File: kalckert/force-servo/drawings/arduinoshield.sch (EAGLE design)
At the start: 20 parts, among them IC1 MCP604P, IC2 7806L

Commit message: Finnished PC board
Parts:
- added X3, X4: (no value), con-phoenix-254:MPT2
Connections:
- net GND: now also X3-1.1, X4-1.1
- net LED_GREEN: now also X3-2.1
- net LED_RED: now also X4-2.1
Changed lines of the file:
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@@
 <part name="R3" library="resistor" deviceset="R-EU_" device="0207/7" value="10k"/>
 <part name="R4" library="resistor" deviceset="R-EU_" device="0207/7" value="10k"/>
+<part name="X3" library="con-phoenix-254" deviceset="MPT2" device="">
+<attribute name="MF" value=""/>
+<attribute name="MPN" value=""/>
+<attribute name="OC_FARNELL" value="unknown"/>
+<attribute name="OC_NEWARK" value="unknown"/>
+</part>
+<part name="X4" library="con-phoenix-254" deviceset="MPT2" device="">
+<attribute name="MF" value=""/>
+<attribute name="MPN" value=""/>
+<attribute name="OC_FARNELL" value="unknown"/>
+<attribute name="OC_NEWARK" value="unknown"/>
+</part>
+<part name="GND5" library="supply1" deviceset="GND" device=""/>
+<part name="GND7" library="supply1" deviceset="GND" device=""/>
 </parts>
 <sheets>
 <sheet>
 <plain>
-<text x="86.36" y="15.24" size="1.778" layer="91">Shield for the Arduino Board</text>
+<text x="205.74" y="20.32" size="1.778" layer="94" font="vector" rot="MR0">Shield for the Arduino Board</text>
 </plain>
 <instances>
@@
 <instance part="R3" gate="G$1" x="195.58" y="114.3"/>
 <instance part="R4" gate="G$1" x="195.58" y="111.76"/>
+<instance part="X3" gate="-1" x="243.84" y="114.3" rot="MR180"/>
+<instance part="X3" gate="-2" x="243.84" y="119.38" smashed="yes" rot="MR180">
+<attribute name="NAME" x="247.396" y="120.015" size="1.778" layer="95" rot="MR180"/>
+<attribute name="VALUE" x="242.824" y="122.682" size="1.778" layer="96" rot="MR180"/>
+</instance>
+<instance part="X4" gate="-1" x="243.84" y="96.52" rot="MR180"/>
+<instance part="X4" gate="-2" x="243.84" y="101.6" smashed="yes" rot="MR180">
+<attribute name="NAME" x="247.396" y="102.235" size="1.778" layer="95" rot="MR180"/>
+<attribute name="VALUE" x="242.824" y="104.902" size="1.778" layer="96" rot="MR180"/>
+</instance>
+<instance part="GND5" gate="1" x="238.76" y="91.44"/>
+<instance part="GND7" gate="1" x="238.76" y="109.22"/>
 </instances>
 <busses>
@@
 <wire x1="73.66" y1="101.6" x2="73.66" y2="99.06" width="0.1524" layer="91"/>
 </segment>
+<segment>
+<pinref part="X4" gate="-1" pin="1"/>
+<wire x1="241.3" y1="96.52" x2="238.76" y2="96.52" width="0.1524" layer="91"/>
+<wire x1="238.76" y1="96.52" x2="238.76" y2="93.98" width="0.1524" layer="91"/>
+<pinref part="GND5" gate="1" pin="GND"/>
+</segment>
+<segment>
+<pinref part="X3" gate="-1" pin="1"/>
+<wire x1="241.3" y1="114.3" x2="238.76" y2="114.3" width="0.1524" layer="91"/>
+<wire x1="238.76" y1="114.3" x2="238.76" y2="111.76" width="0.1524" layer="91"/>
+<pinref part="GND7" gate="1" pin="GND"/>
+</segment>
 </net>
 <net name="VCCSERVO" class="0">
@@
 <label x="203.2" y="114.3" size="1.778" layer="95"/>
 </segment>
+<segment>
+<pinref part="X3" gate="-2" pin="1"/>
+<wire x1="241.3" y1="119.38" x2="238.76" y2="119.38" width="0.1524" layer="91"/>
+<label x="223.52" y="119.38" size="1.778" layer="95"/>
+</segment>
 </net>
 <net name="LED_RED" class="0">
@@
 <label x="203.2" y="111.76" size="1.778" layer="95"/>
 </segment>
-</net>
+<segment>
+<pinref part="X4" gate="-2" pin="1"/>
+<wire x1="241.3" y1="101.6" x2="238.76" y2="101.6" width="0.1524" layer="91"/>
+<label x="223.52" y="101.6" size="1.778" layer="95"/>
+</segment>
+</net>

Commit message: First version of the PCB is ready.
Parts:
- removed 7905: 7905, linear:7905L
- removed IC2: 7806L, linear:7806L
- added IC3: 7806T, linear:7806T
- added IC4: (no value), linear:7905T
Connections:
- net -9V: now also IC4.GND; no longer 7905.GND
- net BUZZER: now also DIGITALPIN0-7.4; no longer DIGITALPIN0-7.1
- net GND: now also IC4.VO; no longer 7905.VO
- net N$1: now also DIGITALPIN0-7.1; no longer DIGITALPIN0-7.3
- net N$2: now also IC4.VI; no longer 7905.VI
- net N$3: now also IC3.GND; no longer IC2.GND
- net N$4: now also DIGITALPIN0-7.2; no longer DIGITALPIN0-7.4
- net VCCSERVO: now also IC3.VO; no longer IC2.VO
- net VIN: now also IC3.VI; no longer IC2.VI
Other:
- moved on the sheet: R3, R4
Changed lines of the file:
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@@
 <setting verticaltext="up"/>
 </settings>
-<grid distance="0.1" unitdist="inch" unit="inch" style="lines" multiple="1" display="yes" altdistance="0.01" altunitdist="inch" altunit="inch"/>
+<grid distance="0.1" unitdist="inch" unit="inch" style="lines" multiple="1" display="no" altdistance="0.01" altunitdist="inch" altunit="inch"/>
 <layers>
 <layer number="1" name="Top" color="4" fill="1" visible="no" active="no"/>
@@
 <part name="SG1" library="buzzer" deviceset="F/HMB" device=""/>
 <part name="IC1" library="linear" deviceset="MCP604" device="P"/>
-<part name="7905" library="linear" deviceset="79*" device="L" technology="05" value="7905"/>
 <part name="R1" library="pot" deviceset="TRIM_EU-" device="S64W"/>
 <part name="C1" library="rcl" deviceset="C-EU" device="025-025X050" value="330nF"/>
@@
 <part name="GND2" library="supply1" deviceset="GND" device=""/>
 <part name="GND4" library="supply1" deviceset="GND" device=""/>
-<part name="IC2" library="linear" deviceset="78*" device="L" technology="06"/>
 <part name="C3" library="rcl" deviceset="C-EU" device="025-025X050" value="330nF"/>
 <part name="C4" library="rcl" deviceset="C-EU" device="025-025X050" value="100nF"/>
@@
 <part name="GND5" library="supply1" deviceset="GND" device=""/>
 <part name="GND7" library="supply1" deviceset="GND" device=""/>
+<part name="IC3" library="linear" deviceset="78*" device="T" technology="06"/>
+<part name="IC4" library="linear" deviceset="79*" device="T" technology="05"/>
 </parts>
 <sheets>
@@
 <instance part="IC1" gate="C" x="170.18" y="35.56"/>
 <instance part="IC1" gate="D" x="198.12" y="35.56"/>
-<instance part="7905" gate="A1" x="53.34" y="33.02"/>
 <instance part="R1" gate="1" x="99.06" y="152.4" rot="R270"/>
 <instance part="C1" gate="G$1" x="33.02" y="35.56"/>
@@
 <instance part="GND2" gate="1" x="73.66" y="96.52"/>
 <instance part="GND4" gate="1" x="142.24" y="66.04"/>
-<instance part="IC2" gate="A1" x="53.34" y="63.5"/>
 <instance part="C3" gate="G$1" x="33.02" y="60.96"/>
 <instance part="C4" gate="G$1" x="68.58" y="60.96"/>
-<instance part="GND3" gate="1" x="53.34" y="53.34"/>
+<instance part="GND3" gate="1" x="53.34" y="48.26"/>
 <instance part="GND6" gate="1" x="68.58" y="27.94"/>
-<instance part="R3" gate="G$1" x="195.58" y="114.3"/>
-<instance part="R4" gate="G$1" x="195.58" y="111.76"/>
+<instance part="R3" gate="G$1" x="195.58" y="119.38"/>
+<instance part="R4" gate="G$1" x="195.58" y="116.84"/>
 <instance part="X3" gate="-1" x="243.84" y="114.3" rot="MR180"/>
 <instance part="X3" gate="-2" x="243.84" y="119.38" smashed="yes" rot="MR180">
@@
 <instance part="GND5" gate="1" x="238.76" y="91.44"/>
 <instance part="GND7" gate="1" x="238.76" y="109.22"/>
+<instance part="IC3" gate="A1" x="53.34" y="63.5"/>
+<instance part="IC4" gate="A1" x="53.34" y="33.02"/>
 </instances>
 <busses>
@@
 <wire x1="33.02" y1="38.1" x2="53.34" y2="38.1" width="0.1524" layer="91"/>
 <junction x="33.02" y="38.1"/>
-<pinref part="7905" gate="A1" pin="GND"/>
-<junction x="53.34" y="38.1"/>
+<junction x="68.58" y="38.1"/>
 <wire x1="53.34" y1="38.1" x2="68.58" y2="38.1" width="0.1524" layer="91"/>
-<junction x="68.58" y="38.1"/>
 <wire x1="68.58" y1="38.1" x2="76.2" y2="38.1" width="0.1524" layer="91"/>
 <label x="76.2" y="38.1" size="1.778" layer="95"/>
 <wire x1="33.02" y1="38.1" x2="27.94" y2="38.1" width="0.1524" layer="91"/>
+<pinref part="IC4" gate="A1" pin="GND"/>
+<junction x="53.34" y="38.1"/>
 </segment>
 <segment>
@@
 <pinref part="C1" gate="G$1" pin="2"/>
 <pinref part="BATTERY" gate="-2" pin="1"/>
-<pinref part="7905" gate="A1" pin="VI"/>
 <wire x1="33.02" y1="30.48" x2="43.18" y2="30.48" width="0.1524" layer="91"/>
 <junction x="33.02" y="30.48"/>
 <wire x1="33.02" y1="30.48" x2="27.94" y2="30.48" width="0.1524" layer="91"/>
+<pinref part="IC4" gate="A1" pin="VI"/>
 </segment>
 </net>
@@
 <segment>
 <pinref part="C2" gate="G$1" pin="2"/>
-<pinref part="7905" gate="A1" pin="VO"/>
 <wire x1="68.58" y1="30.48" x2="63.5" y2="30.48" width="0.1524" layer="91"/>
 <junction x="68.58" y="30.48"/>
 <pinref part="GND6" gate="1" pin="GND"/>
+<pinref part="IC4" gate="A1" pin="VO"/>
 </segment>
 <segment>
@@
 </segment>
 <segment>
-<pinref part="IC2" gate="A1" pin="VO"/>
 <wire x1="63.5" y1="63.5" x2="68.58" y2="63.5" width="0.1524" layer="91"/>
 <pinref part="C4" gate="G$1" pin="1"/>
@@
 <junction x="68.58" y="63.5"/>
 <label x="73.66" y="63.5" size="1.778" layer="95"/>
+<pinref part="IC3" gate="A1" pin="VO"/>
 </segment>
 </net>
@@
 </segment>
 <segment>
-<pinref part="DIGITALPIN0-7" gate="A" pin="1"/>
-<wire x1="185.42" y1="119.38" x2="195.58" y2="119.38" width="0.1524" layer="91"/>
-<label x="195.58" y="119.38" size="1.778" layer="95"/>
+<pinref part="DIGITALPIN0-7" gate="A" pin="4"/>
+<wire x1="185.42" y1="111.76" x2="203.2" y2="111.76" width="0.1524" layer="91"/>
+<label x="203.2" y="111.76" size="1.778" layer="95"/>
 </segment>
 </net>
@@
 </segment>
 <segment>
-<pinref part="IC2" gate="A1" pin="VI"/>
 <wire x1="43.18" y1="63.5" x2="33.02" y2="63.5" width="0.1524" layer="91"/>
 <pinref part="C3" gate="G$1" pin="1"/>
@@
 <junction x="33.02" y="63.5"/>
 <label x="25.4" y="63.5" size="1.778" layer="95"/>
+<pinref part="IC3" gate="A1" pin="VI"/>
 </segment>
 </net>
 <net name="N$3" class="0">
 <segment>
+<pinref part="GND3" gate="1" pin="GND"/>
+<pinref part="IC3" gate="A1" pin="GND"/>
+<wire x1="53.34" y1="50.8" x2="53.34" y2="53.34" width="0.1524" layer="91"/>
 <pinref part="C3" gate="G$1" pin="2"/>
-<wire x1="33.02" y1="55.88" x2="53.34" y2="55.88" width="0.1524" layer="91"/>
+<wire x1="53.34" y1="53.34" x2="53.34" y2="55.88" width="0.1524" layer="91"/>
+<wire x1="33.02" y1="55.88" x2="33.02" y2="53.34" width="0.1524" layer="91"/>
 <pinref part="C4" gate="G$1" pin="2"/>
-<pinref part="GND3" gate="1" pin="GND"/>
-<wire x1="53.34" y1="55.88" x2="68.58" y2="55.88" width="0.1524" layer="91"/>
-<junction x="53.34" y="55.88"/>
-<pinref part="IC2" gate="A1" pin="GND"/>
-</segment>
-</net>
-<net name="N$4" class="0">
-<segment>
-<pinref part="R4" gate="G$1" pin="1"/>
-<pinref part="DIGITALPIN0-7" gate="A" pin="4"/>
-<wire x1="190.5" y1="111.76" x2="185.42" y2="111.76" width="0.1524" layer="91"/>
+<wire x1="33.02" y1="53.34" x2="53.34" y2="53.34" width="0.1524" layer="91"/>
+<wire x1="53.34" y1="53.34" x2="68.58" y2="53.34" width="0.1524" layer="91"/>
+<wire x1="68.58" y1="53.34" x2="68.58" y2="55.88" width="0.1524" layer="91"/>
+<junction x="53.34" y="53.34"/>
 </segment>
 </net>
@@
 <segment>
 <pinref part="R3" gate="G$1" pin="2"/>
-<wire x1="200.66" y1="114.3" x2="203.2" y2="114.3" width="0.1524" layer="91"/>
-<label x="203.2" y="114.3" size="1.778" layer="95"/>
+<wire x1="200.66" y1="119.38" x2="203.2" y2="119.38" width="0.1524" layer="91"/>
+<label x="203.2" y="119.38" size="1.778" layer="95"/>
 </segment>
 <segment>
@@
 <segment>
 <pinref part="R4" gate="G$1" pin="2"/>
-<wire x1="200.66" y1="111.76" x2="203.2" y2="111.76" width="0.1524" layer="91"/>
-<label x="203.2" y="111.76" size="1.778" layer="95"/>
+<wire x1="200.66" y1="116.84" x2="203.2" y2="116.84" width="0.1524" layer="91"/>
+<label x="203.2" y="116.84" size="1.778" layer="95"/>
 </segment>
 <segment>
@@
 <segment>
 <pinref part="R3" gate="G$1" pin="1"/>
-<pinref part="DIGITALPIN0-7" gate="A" pin="3"/>
-<wire x1="190.5" y1="114.3" x2="185.42" y2="114.3" width="0.1524" layer="91"/>
-</segment>
-</net>
+<pinref part="DIGITALPIN0-7" gate="A" pin="1"/>
+<wire x1="190.5" y1="119.38" x2="185.42" y2="119.38" width="0.1524" layer="91"/>
+</segment>
+</net>
+<net name="N$4" class="0">
+<segment>
+<pinref part="DIGITALPIN0-7" gate="A" pin="2"/>
+<pinref part="R4" gate="G$1" pin="1"/>
+<wire x1="185.42" y1="116.84" x2="190.5" y2="116.84" width="0.1524" layer="91"/>
+</segment>
+</net>

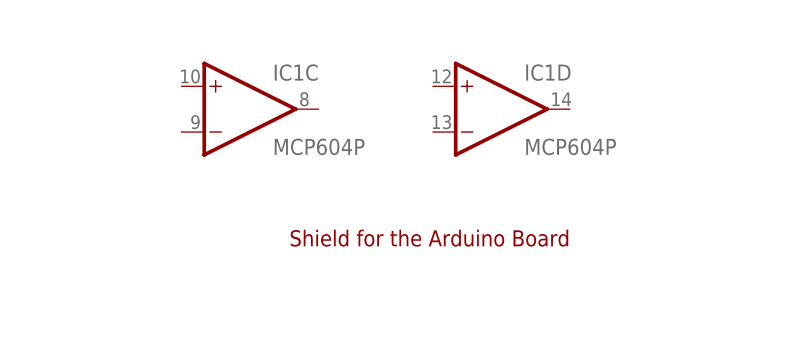
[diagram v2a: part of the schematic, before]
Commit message: Added licensing info to board. Tested python program on mac (tkinter only works in IDLE).
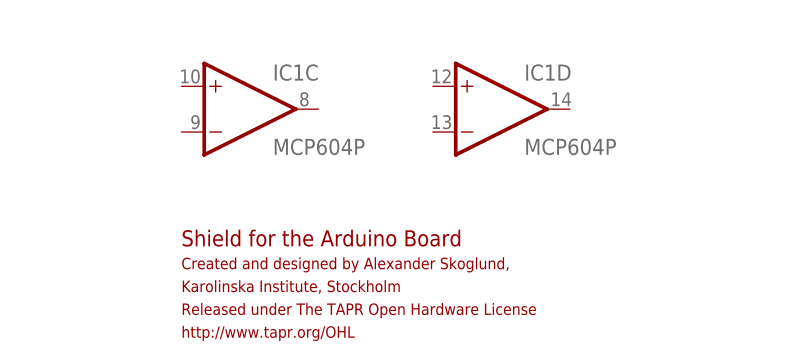
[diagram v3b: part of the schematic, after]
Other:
- note added: "Created and designed by Alexander Skoglund,"
- note added: "Karolinska Institute, Stockholm"
- note added: "Released under The TAPR Open Hardware License"
- note added: "http://www.tapr.org/OHL"
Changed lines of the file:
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@@
 <sheet>
 <plain>
-<text x="205.74" y="20.32" size="1.778" layer="94" font="vector" rot="MR0">Shield for the Arduino Board</text>
+<text x="162.56" y="20.32" size="1.778" layer="94" font="vector" rot="MR0" align="bottom-right">Shield for the Arduino Board</text>
+<text x="162.56" y="17.78" size="1.27" layer="94" font="vector" rot="MR0" align="bottom-right">Created and designed by Alexander Skoglund,</text>
+<text x="162.56" y="15.24" size="1.27" layer="94" font="vector" rot="MR0" align="bottom-right">Karolinska Institute, Stockholm</text>
+<text x="162.56" y="12.7" size="1.27" layer="94" font="vector" rot="MR0" align="bottom-right">Released under The TAPR Open Hardware License</text>
+<text x="162.56" y="10.16" size="1.27" layer="94" font="vector" rot="MR0" align="bottom-right">http://www.tapr.org/OHL</text>
 </plain>
 <instances>

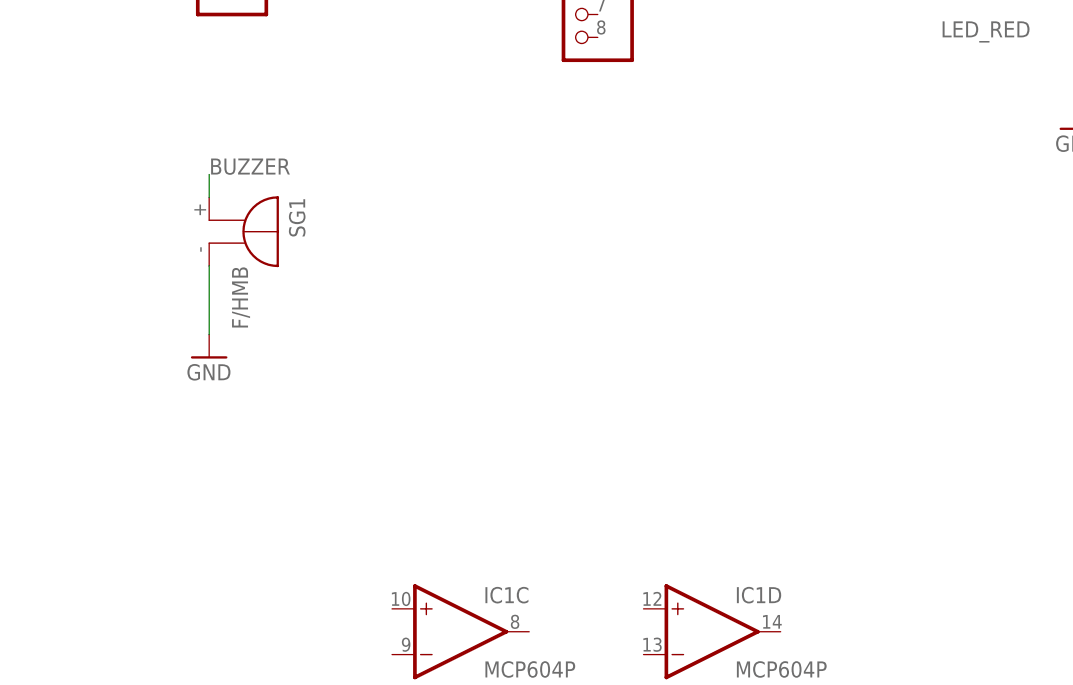
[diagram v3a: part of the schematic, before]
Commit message: Added a timestamp to the measure, ms from start of prog.
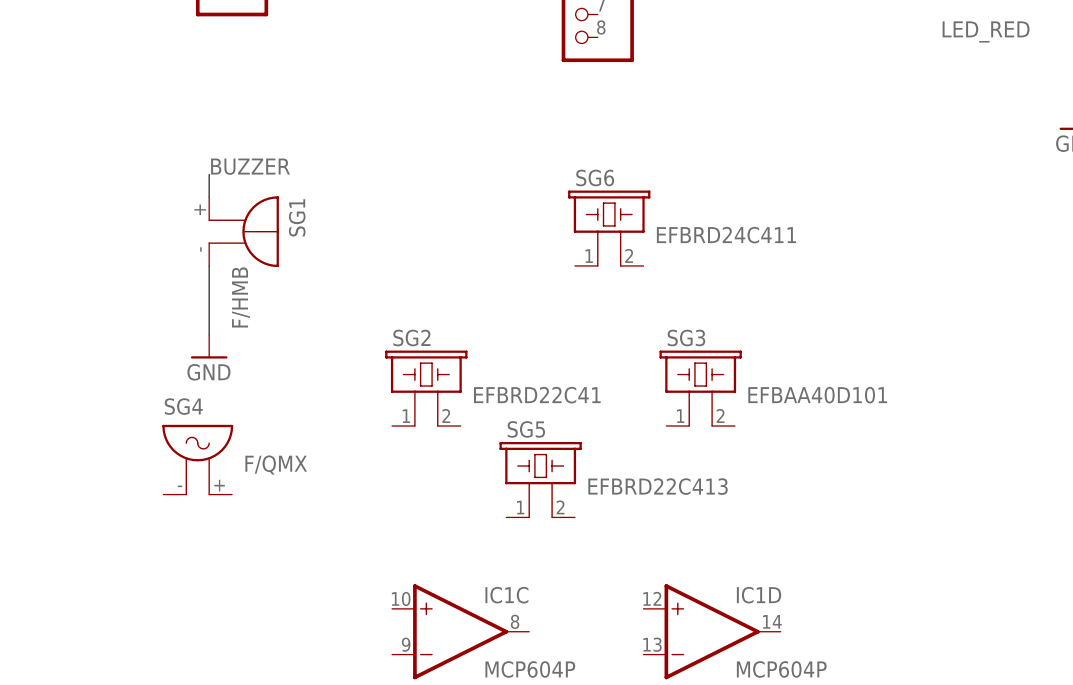
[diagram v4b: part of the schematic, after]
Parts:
- added SG2: EFBRD22C41, buzzer:EFBRD22C41
- added SG3: EFBAA40D101, buzzer:EFBAA40D101
- added SG4: F/QMX, buzzer:F/QMX
- added SG5: EFBRD22C413, buzzer:EFBRD22C413
- added SG6: EFBRD24C411, buzzer:EFBRD24C411
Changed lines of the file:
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@@
 <part name="IC3" library="linear" deviceset="78*" device="T" technology="06"/>
 <part name="IC4" library="linear" deviceset="79*" device="T" technology="05"/>
+<part name="SG4" library="buzzer" deviceset="F/QMX" device=""/>
+<part name="SG2" library="buzzer" deviceset="EFB?" device="RD22C41"/>
+<part name="SG3" library="buzzer" deviceset="EFB?" device="AA40D101"/>
+<part name="SG5" library="buzzer" deviceset="EFB?" device="RD22C413"/>
+<part name="SG6" library="buzzer" deviceset="EFB?" device="RD24C411"/>
 </parts>
 <sheets>
@@
 <instance part="IC3" gate="A1" x="53.34" y="63.5"/>
 <instance part="IC4" gate="A1" x="53.34" y="33.02"/>
+<instance part="SG4" gate="G$1" x="139.7" y="53.34"/>
+<instance part="SG2" gate="G$1" x="165.1" y="60.96"/>
+<instance part="SG3" gate="G$1" x="195.58" y="60.96"/>
+<instance part="SG5" gate="G$1" x="177.8" y="50.8"/>
+<instance part="SG6" gate="G$1" x="185.42" y="78.74"/>
 </instances>
 <busses>
